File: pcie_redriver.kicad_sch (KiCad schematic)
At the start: 0 parts

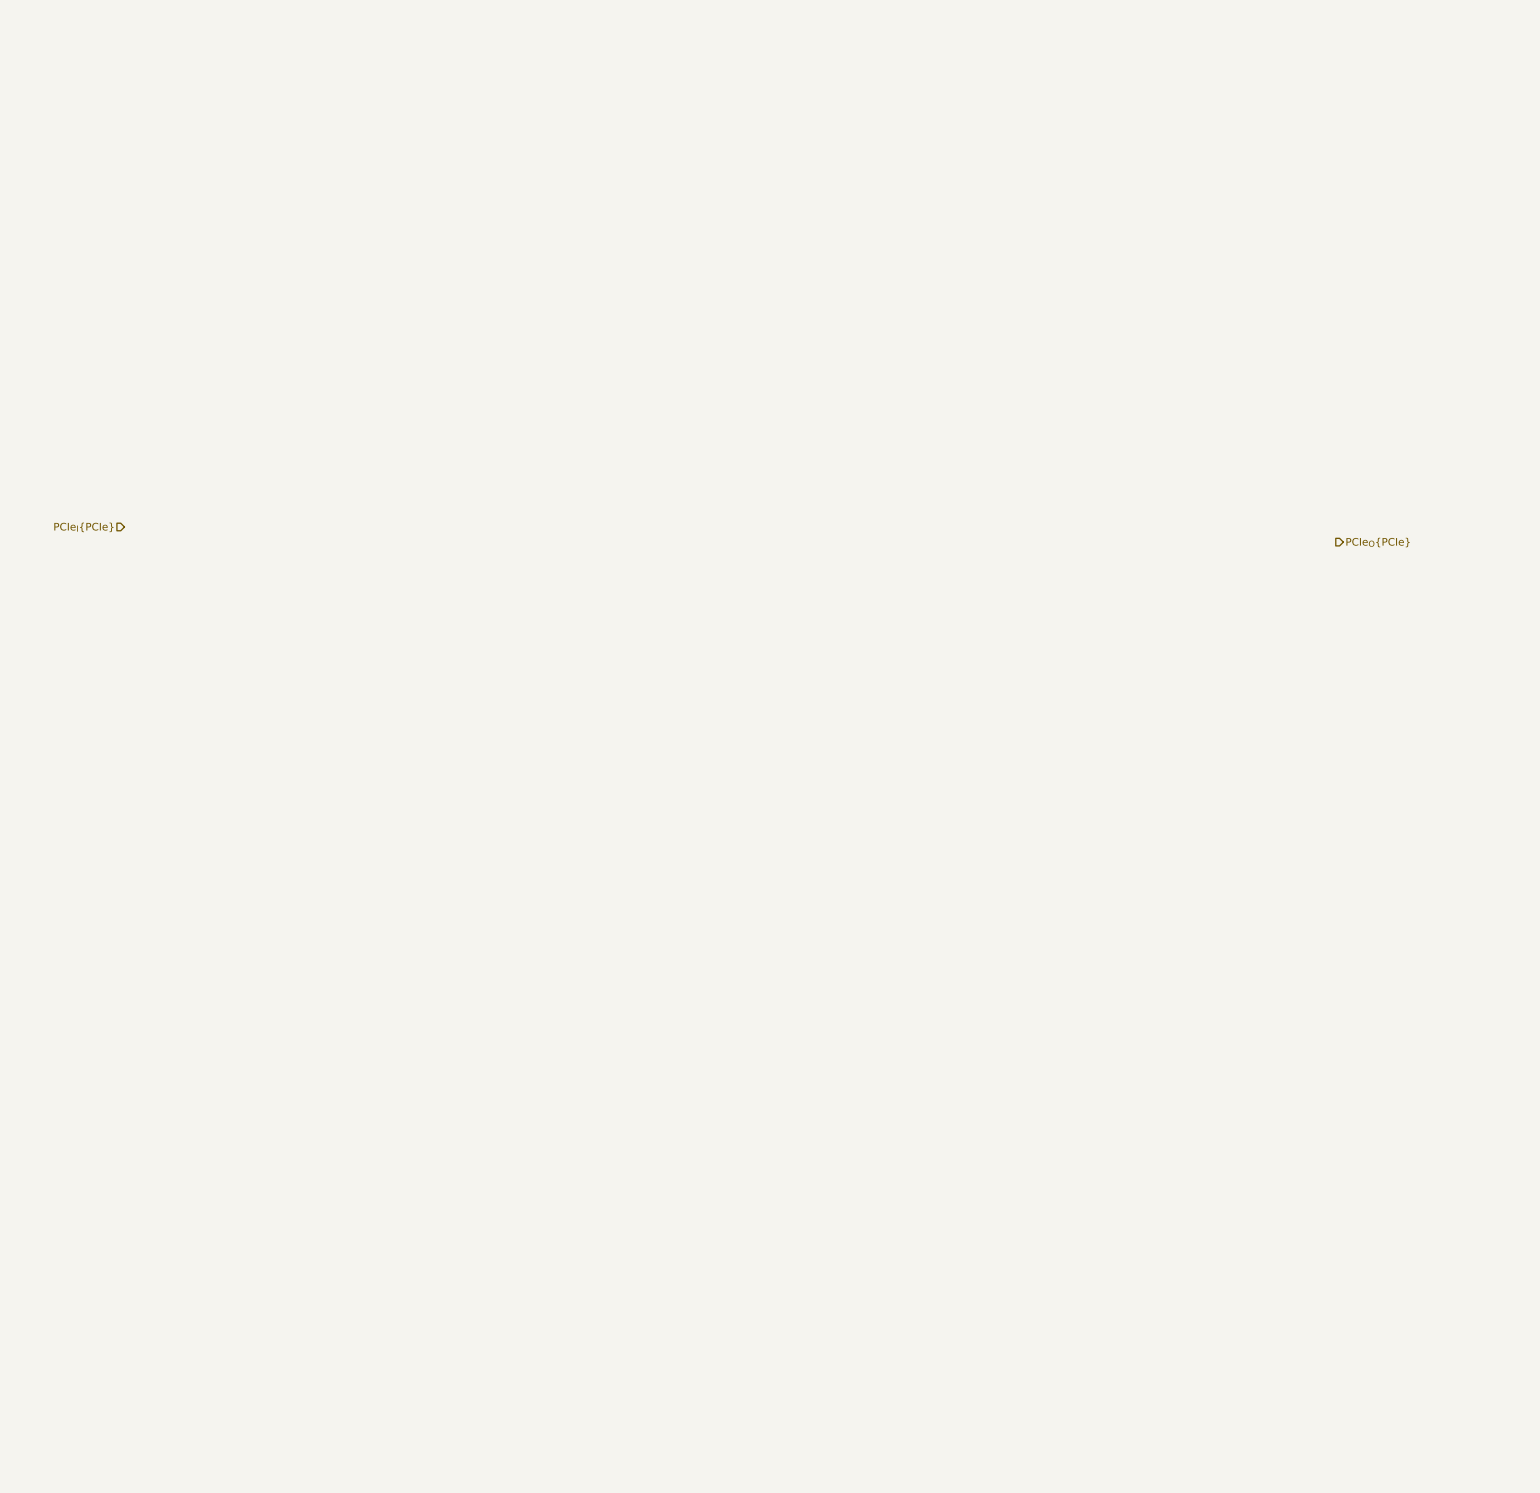
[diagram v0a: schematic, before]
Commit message: [#57056] Add PCIe redriver for OCuLink
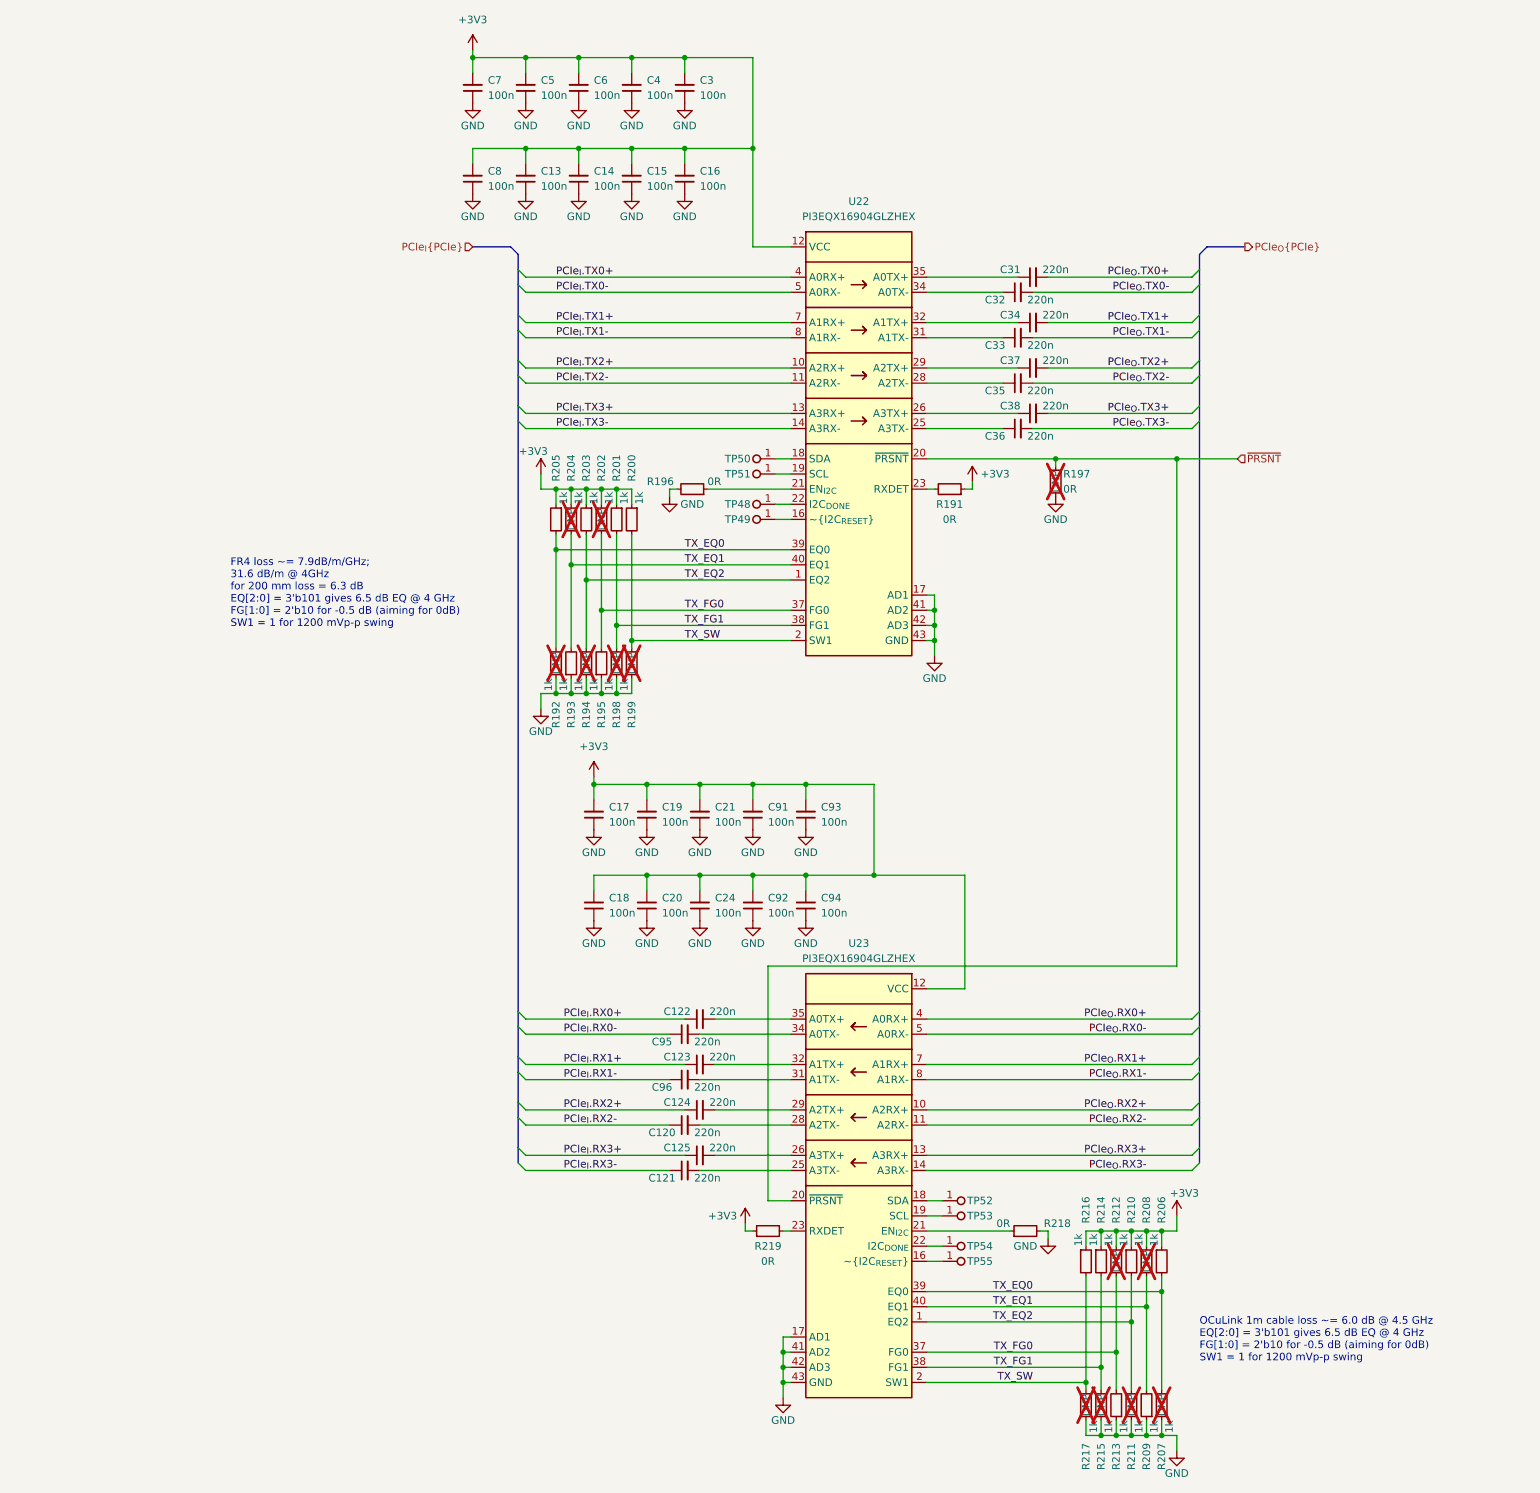
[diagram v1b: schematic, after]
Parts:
- added C120, C121, C122, C123, C124, C125, C31, C32, C33, C34, C35, C36, C37, C38, C95, C96: C_220n_0402, antmicro-footprints:C_0402_1005Metric, symbol antmicroCapacitors0402:C_220n_0402
- added C13, C14, C15, C16, C17, C18, C19, C20, C21, C24, C3, C4, C5, C6, C7, C8, C91, C92, C93, C94: C_100n_0402, antmicro-footprints:C_0402_1005Metric, symbol antmicroCapacitors0402:C_100n_0402
- added R191, R196, R197, R218, R219: R_0R_0402, antmicro-footprints:R_0402_1005Metric, symbol antmicroResistors0402:R_0R_0402
- added R192, R193, R194, R195, R198, R199, R200, R201, R202, R203, R204, R205, R206, R207, R208, R209, R210, R211, R212, R213, R214, R215, R216, R217: R_1k_0402, antmicro-footprints:R_0402_1005Metric, symbol antmicroResistors0402:R_1k_0402
- added TP48, TP49, TP50, TP51, TP52, TP53, TP54, TP55: TP_0.75mm_SMD, antmicro-footprints:TP_SMD_0.75mm, symbol antmicroTestPoints:TP_0.75mm_SMD
- added U22, U23: PI3EQX16904GL, antmicro-footprints:WQFN-42-1EP_3.5x9mm_P0.5mm, symbol antmicroInterfaceDriversReceiversTransceivers:PI3EQX16904GL
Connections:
- new net: C35.1, U22.28 (A2TX-)
- new net: C34.1, U22.32 (A1TX+)
- new net: C38.1, U22.26 (A3TX+)
- new net: C32.1, U22.34 (A0TX-)
- new net: R196.1, U22.21 (EN_{I2C})
- new net: TP53.1, U23.19 (SCL)
- new net: TP55.1, U23.16 (~{I2C_{RESET}})
- new net: TP48.1, U22.22 (I2C_{DONE})
- new net: TP50.1, U22.18 (SDA)
- new net: C121.2, U23.25 (A3TX-)
- new net: C33.1, U22.31 (A1TX-)
- new net: C36.1, U22.25 (A3TX-)
- new net: C31.1, U22.35 (A0TX+)
- new net: TP51.1, U22.19 (SCL)
- new net: R191.2, U22.23 (RXDET)
- new net: R218.1, U23.21 (EN_{I2C})
- new net: TP52.1, U23.18 (SDA)
- new net: TP54.1, U23.22 (I2C_{DONE})
- new net: R219.2, U23.23 (RXDET)
- new net: C125.2, U23.26 (A3TX+)
- new net: C120.2, U23.28 (A2TX-)
- new net: C124.2, U23.29 (A2TX+)
- new net: C96.2, U23.31 (A1TX-)
- new net: C123.2, U23.32 (A1TX+)
- new net: C95.2, U23.34 (A0TX-)
- new net: C122.2, U23.35 (A0TX+)
- new net: TP49.1, U22.16 (~{I2C_{RESET}})
- new net: C37.1, U22.29 (A2TX+)
- new net +3V3: C13.2, C14.2, C15.2, C16.2, C17.2, C18.2, C19.2, C20.2, C21.2, C24.2, C3.2, C4.2, C5.2, C6.2, C7.2, C8.2, C91.2, C92.2, C93.2, C94.2, R191.1, R200.1, R201.1, R202.1, R203.1, R204.1, R205.1, R206.1, R208.1, R210.1, R212.1, R214.1, R216.1, R219.1, U22.12 (VCC), U22.15 (VCC), U22.24 (VCC), U22.27 (VCC), U22.3 (VCC), U22.30 (VCC), U22.33 (VCC), U22.36 (VCC), U22.6 (VCC), U22.9 (VCC), U23.12 (VCC), U23.15 (VCC), U23.24 (VCC), U23.27 (VCC), U23.3 (VCC), U23.30 (VCC), U23.33 (VCC), U23.36 (VCC), U23.6 (VCC), U23.9 (VCC)
- new net GND: C13.1, C14.1, C15.1, C16.1, C17.1, C18.1, C19.1, C20.1, C21.1, C24.1, C3.1, C4.1, C5.1, C6.1, C7.1, C8.1, C91.1, C92.1, C93.1, C94.1, R192.1, R193.1, R194.1, R195.1, R196.2, R197.1, R198.1, R199.1, R207.1, R209.1, R211.1, R213.1, R215.1, R217.1, R218.2, U22.17 (AD1), U22.41 (AD2), U22.42 (AD3), U22.43 (GND), U23.17 (AD1), U23.41 (AD2), U23.42 (AD3), U23.43 (GND)
- new net PCIe_{I}.RX0+: C122.1
- new net PCIe_{I}.RX0-: C95.1
- new net PCIe_{I}.RX1+: C123.1
- new net PCIe_{I}.RX1-: C96.1
- new net PCIe_{I}.RX2+: C124.1
- new net PCIe_{I}.RX2-: C120.1
- new net PCIe_{I}.RX3+: C125.1
- new net PCIe_{I}.RX3-: C121.1
- new net PCIe_{I}.TX0+: U22.4 (A0RX+)
- new net PCIe_{I}.TX0-: U22.5 (A0RX-)
- new net PCIe_{I}.TX1+: U22.7 (A1RX+)
- new net PCIe_{I}.TX1-: U22.8 (A1RX-)
- new net PCIe_{I}.TX2+: U22.10 (A2RX+)
- new net PCIe_{I}.TX2-: U22.11 (A2RX-)
- new net PCIe_{I}.TX3+: U22.13 (A3RX+)
- new net PCIe_{I}.TX3-: U22.14 (A3RX-)
- new net PCIe_{O}.RX0+: U23.4 (A0RX+)
- new net PCIe_{O}.RX0-: U23.5 (A0RX-)
- new net PCIe_{O}.RX1+: U23.7 (A1RX+)
- new net PCIe_{O}.RX1-: U23.8 (A1RX-)
- new net PCIe_{O}.RX2+: U23.10 (A2RX+)
- new net PCIe_{O}.RX2-: U23.11 (A2RX-)
- new net PCIe_{O}.RX3+: U23.13 (A3RX+)
- new net PCIe_{O}.RX3-: U23.14 (A3RX-)
- new net PCIe_{O}.TX0+: C31.2
- new net PCIe_{O}.TX0-: C32.2
- new net PCIe_{O}.TX1+: C34.2
- new net PCIe_{O}.TX1-: C33.2
- new net PCIe_{O}.TX2+: C37.2
- new net PCIe_{O}.TX2-: C35.2
- new net PCIe_{O}.TX3+: C38.2
- new net PCIe_{O}.TX3-: C36.2
- new net TX_EQ0: R192.2, R205.2, R206.2, R207.2, U22.39 (EQ0), U23.39 (EQ0)
- new net TX_EQ1: R193.2, R204.2, R208.2, R209.2, U22.40 (EQ1), U23.40 (EQ1)
- new net TX_EQ2: R194.2, R203.2, R210.2, R211.2, U22.1 (EQ2), U23.1 (EQ2)
- new net TX_FG0: R195.2, R202.2, R212.2, R213.2, U22.37 (FG0), U23.37 (FG0)
- new net TX_FG1: R198.2, R201.2, R214.2, R215.2, U22.38 (FG1), U23.38 (FG1)
- new net TX_SW: R199.2, R200.2, R216.2, R217.2, U22.2 (SW1), U23.2 (SW1)
- new net ~{PRSNT}: R197.2, U22.20 (~{PRSNT}), U23.20 (~{PRSNT})
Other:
- note added: "FR4 loss ~= 7.9dB/m/GHz; 31.6 dB/m @ 4GHz for 200 mm loss = 6.3 dB EQ[2:0] = 3'b101 gives 6.5 dB EQ @ 4 GHz FG[1:0] = 2'b10 for -0.5 dB (aiming for 0dB) SW1 = 1 for 1200 mVp-p swing"
- note added: "OCuLink 1m cable loss ~= 6.0 dB @ 4.5 GHz EQ[2:0] = 3'b101 gives 6.5 dB EQ @ 4 GHz FG[1:0] = 2'b10 for -0.5 dB (aiming for 0dB) SW1 = 1 for 1200 mVp-p swing"

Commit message: [#58137] Update backplane connector pinout
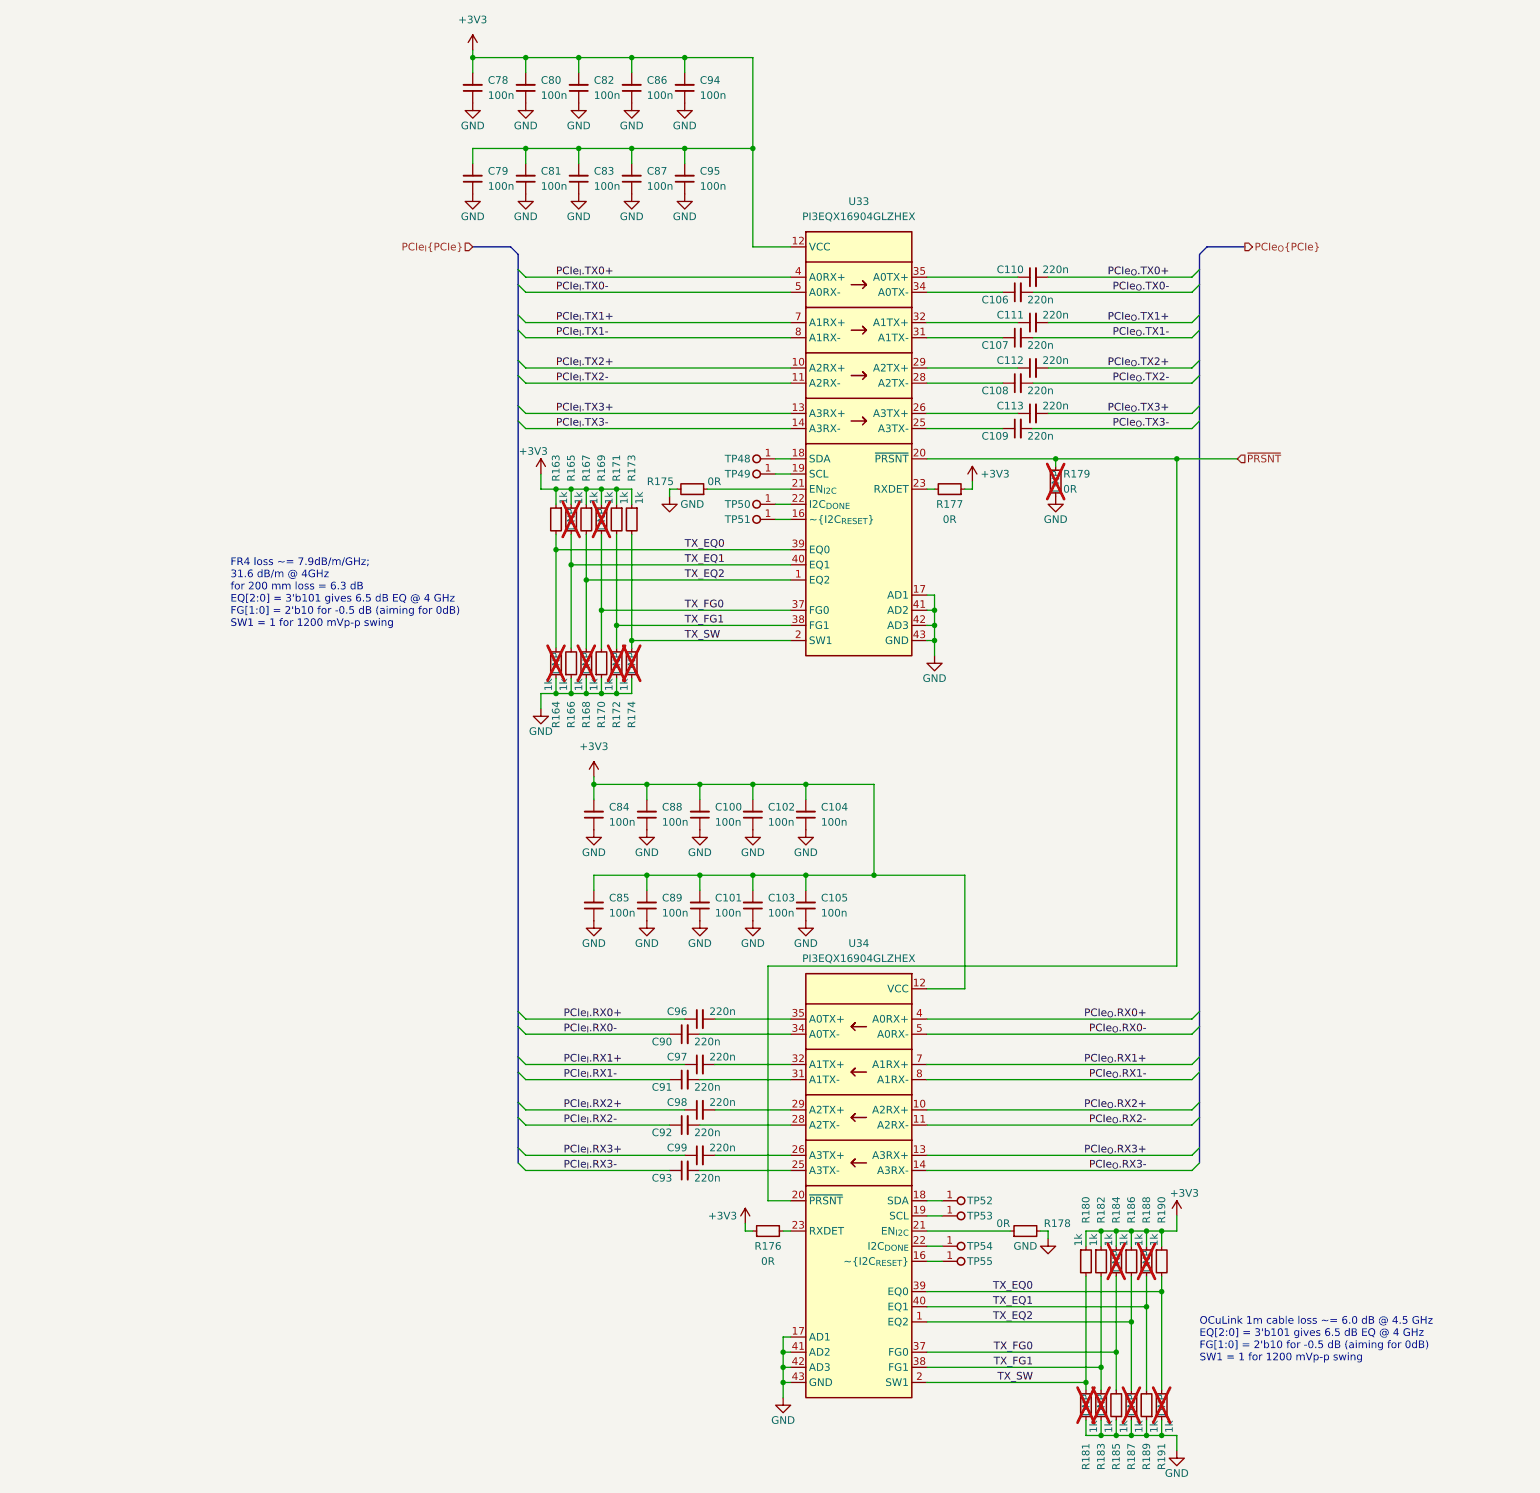
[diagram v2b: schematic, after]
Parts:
- renumbered C21 to C100, C24 to C101, C91 to C102, C92 to C103, C93 to C104, C94 to C105, C32 to C106, C33 to C107, C35 to C108, C36 to C109, C31 to C110, C34 to C111, C37 to C112, C38 to C113, C7 to C78, C8 to C79, C5 to C80, C13 to C81, C6 to C82, C14 to C83, C17 to C84, C18 to C85, C4 to C86, C15 to C87, C19 to C88, C20 to C89, C95 to C90, C96 to C91, C120 to C92, C121 to C93, C3 to C94, C16 to C95, C122 to C96, C123 to C97, C124 to C98, C125 to C99, R205 to R163, R192 to R164, R204 to R165, R193 to R166, R203 to R167, R194 to R168, R202 to R169, R195 to R170, R201 to R171, R198 to R172, R200 to R173, R199 to R174, R196 to R175, R219 to R176, R191 to R177, R218 to R178, R197 to R179, R216 to R180, R217 to R181, R214 to R182, R215 to R183, R212 to R184, R213 to R185, R210 to R186, R211 to R187, R208 to R188, R209 to R189, R206 to R190, R207 to R191, TP50 to TP48, TP51 to TP49, TP48 to TP50, TP49 to TP51, U22 to U33, U23 to U34
